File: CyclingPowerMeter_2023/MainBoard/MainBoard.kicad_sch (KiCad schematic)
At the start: 34 parts, among them J1 Conn_01x01, J10 S2B-PH-SM4-TB_LF__SN_, J11 Conn_01x01, J12 Conn_01x01, J2 Conn_01x01, J3 Conn_01x01, J4 Conn_01x01, J5 Conn_01x01, J6 Conn_01x01, J7 Conn_01x01, J8 Conn_01x01, J9 BLA05-05S30, SW1 RS_PRO_PCB_Slide_Switch_SPDT_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, U1 ADS122U04IPW, U2 Seeed_Studio_XIAO_nRF52840_Se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

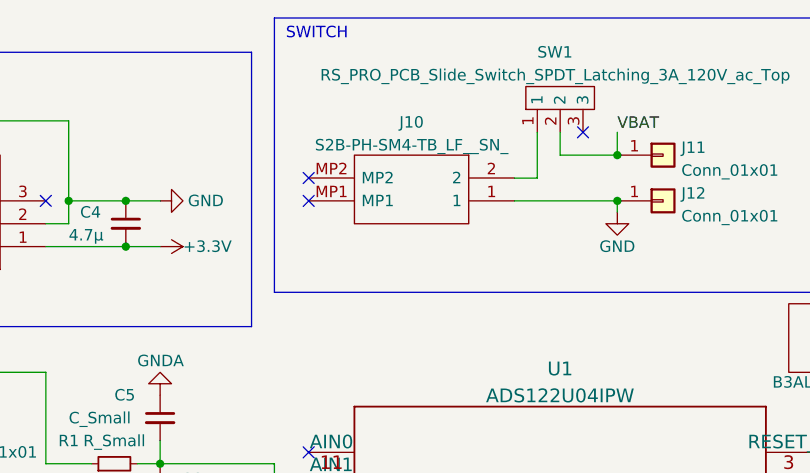
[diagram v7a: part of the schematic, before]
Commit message: 端面スルーホールのオフセットを調整
端面スルーホールのオフセットを調整
PHコネクタの結線を逆にした
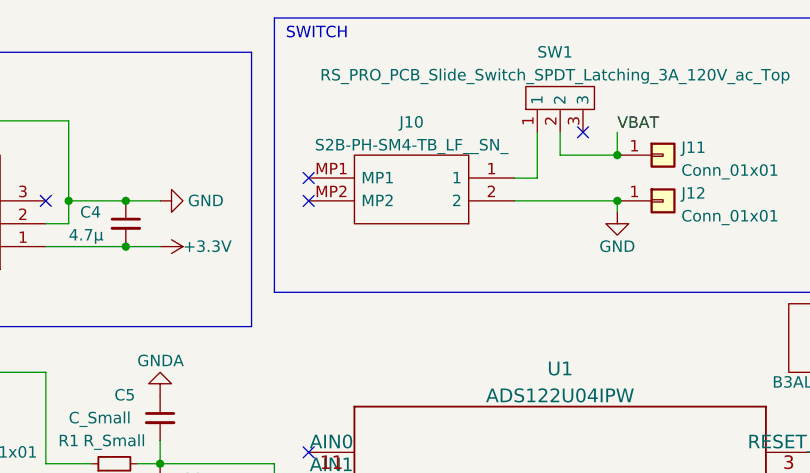
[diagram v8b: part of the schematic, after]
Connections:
- net GND: now also J10.2; no longer J10.1
- net at SW1.1: now also J10.1; no longer J10.2
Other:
- moved on the sheet: J10
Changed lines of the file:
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@@
+    (stroke (width 0) (type default) (color 0 0 0 0))
+  )
+  (wire (pts (xy 142.24 55.88) (xy 153.67 55.88))
     (stroke (width 0) (type default) (color 0 0 0 0))
   )
@@
     (stroke (width 0) (type default) (color 0 0 0 0))
   )
+  (wire (pts (xy 102.87 90.17) (xy 102.87 92.71))
+    (stroke (width 0) (type default) (color 0 0 0 0))
+  )
+  (wire (pts (xy 176.53 116.84) (xy 175.26 116.84))
+    (stroke (width 0) (type default) (color 0 0 0 0))
+  )
+  (wire (pts (xy 144.78 48.26) (xy 144.78 53.34))
+    (stroke (width 0) (type default) (color 0 0 0 0))
+  )
+  (wire (pts (xy 99.06 55.88) (xy 102.87 55.88))
+    (stroke (width 0) (type default) (color 0 0 0 0))
+  )
+  (wire (pts (xy 115.57 90.17) (xy 115.57 88.9))
+    (stroke (width 0) (type default) (color 0 0 0 0))
+  )
+  (wire (pts (xy 92.71 58.42) (xy 92.71 55.88))
+    (stroke (width 0) (type default) (color 0 0 0 0))
+  )
+  (wire (pts (xy 191.77 63.5) (xy 193.04 63.5))
+    (stroke (width 0) (type default) (color 0 0 0 0))
+  )
+  (polyline (pts (xy 115.57 35.56) (xy 176.53 35.56))
+    (stroke (width 0) (type default) (color 0 0 0 0))
+  )
+  (wire (pts (xy 73.66 46.99) (xy 92.71 46.99))
+    (stroke (width 0) (type default) (color 0 0 0 0))
+  )
+  (wire (pts (xy 41.91 55.88) (xy 48.26 55.88))
+    (stroke (width 0) (type default) (color 0 0 0 0))
+  )
+  (wire (pts (xy 64.77 87.63) (xy 72.39 87.63))
+    (stroke (width 0) (type default) (color 0 0 0 0))
+  )
+  (wire (pts (xy 184.15 104.14) (xy 186.69 104.14))
+    (stroke (width 0) (type default) (color 0 0 0 0))
+  )
+  (wire (pts (xy 72.39 87.63) (xy 74.93 87.63))
+    (stroke (width 0) (type default) (color 0 0 0 0))
+  )
+  (wire (pts (xy 187.96 72.39) (xy 190.5 72.39))
+    (stroke (width 0) (type default) (color 0 0 0 0))
+  )
+  (wire (pts (xy 147.32 48.26) (xy 147.32 50.8))
+    (stroke (width 0) (type default) (color 0 0 0 0))
+  )
+  (wire (pts (xy 52.07 87.63) (xy 55.88 83.82))
+    (stroke (width 0) (type default) (color 0 0 0 0))
+  )
+  (polyline (pts (xy 33.02 39.37) (xy 33.02 69.85))
+    (stroke (width 0) (type default) (color 0 0 0 0))
+  )
   (wire (pts (xy 142.24 53.34) (xy 144.78 53.34))
-    (stroke (width 0) (type default) (color 0 0 0 0))
-  )
-  (wire (pts (xy 102.87 90.17) (xy 102.87 92.71))
-    (stroke (width 0) (type default) (color 0 0 0 0))
-  )
-  (wire (pts (xy 176.53 116.84) (xy 175.26 116.84))
-    (stroke (width 0) (type default) (color 0 0 0 0))
-  )
-  (wire (pts (xy 144.78 48.26) (xy 144.78 53.34))
-    (stroke (width 0) (type default) (color 0 0 0 0))
-  )
-  (wire (pts (xy 142.24 55.88) (xy 153.67 55.88))
-    (stroke (width 0) (type default) (color 0 0 0 0))
-  )
-  (wire (pts (xy 99.06 55.88) (xy 102.87 55.88))
-    (stroke (width 0) (type default) (color 0 0 0 0))
-  )
-  (wire (pts (xy 115.57 90.17) (xy 115.57 88.9))
-    (stroke (width 0) (type default) (color 0 0 0 0))
-  )
-  (wire (pts (xy 92.71 58.42) (xy 92.71 55.88))
-    (stroke (width 0) (type default) (color 0 0 0 0))
-  )
-  (wire (pts (xy 191.77 63.5) (xy 193.04 63.5))
-    (stroke (width 0) (type default) (color 0 0 0 0))
-  )
-  (polyline (pts (xy 115.57 35.56) (xy 176.53 35.56))
-    (stroke (width 0) (type default) (color 0 0 0 0))
-  )
-  (wire (pts (xy 73.66 46.99) (xy 92.71 46.99))
-    (stroke (width 0) (type default) (color 0 0 0 0))
-  )
-  (wire (pts (xy 41.91 55.88) (xy 48.26 55.88))
-    (stroke (width 0) (type default) (color 0 0 0 0))
-  )
-  (wire (pts (xy 64.77 87.63) (xy 72.39 87.63))
-    (stroke (width 0) (type default) (color 0 0 0 0))
-  )
-  (wire (pts (xy 184.15 104.14) (xy 186.69 104.14))
-    (stroke (width 0) (type default) (color 0 0 0 0))
-  )
-  (wire (pts (xy 72.39 87.63) (xy 74.93 87.63))
-    (stroke (width 0) (type default) (color 0 0 0 0))
-  )
-  (wire (pts (xy 187.96 72.39) (xy 190.5 72.39))
-    (stroke (width 0) (type default) (color 0 0 0 0))
-  )
-  (wire (pts (xy 147.32 48.26) (xy 147.32 50.8))
-    (stroke (width 0) (type default) (color 0 0 0 0))
-  )
-  (wire (pts (xy 52.07 87.63) (xy 55.88 83.82))
-    (stroke (width 0) (type default) (color 0 0 0 0))
-  )
-  (polyline (pts (xy 33.02 39.37) (xy 33.02 69.85))
     (stroke (width 0) (type default) (color 0 0 0 0))
   )
@@
     (pin "2")
   )
-  (symbol (lib_id "S2B-PH-SM4-TB:S2B-PH-SM4-TB_LF__SN_") (at 142.24 53.34 0) (mirror y) (unit 1)
+  (symbol (lib_id "S2B-PH-SM4-TB:S2B-PH-SM4-TB_LF__SN_") (at 142.24 55.88 180) (unit 1)
     (in_bom yes) (on_board yes) (fields_autoplaced)
     (property "Reference" "J10" (id 0) (at 130.81 47.151 0))
     (property "Value" "S2B-PH-SM4-TB_LF__SN_" (id 1) (at 130.81 49.6879 0))
-    (property "Footprint" "S2B-PH-SM4-TB:S2B-PH-SM4-TB" (id 2) (at 123.19 50.8 0)
-      (effects (font (size 1.27 1.27)) (justify left) hide)
-    )
-    (property "Datasheet" "https://www.jst-mfg.com/product/pdf/eng/ePH.pdf" (id 3) (at 123.19 53.34 0)
-      (effects (font (size 1.27 1.27)) (justify left) hide)
-    )
-    (property "Description" "Conn Shrouded Header (4 Sides) HDR 2 POS 2mm Solder RA Side Entry SMD T/R" (id 4) (at 123.19 55.88 0)
-      (effects (font (size 1.27 1.27)) (justify left) hide)
-    )
-    (property "Height" "6.6" (id 5) (at 123.19 58.42 0)
-      (effects (font (size 1.27 1.27)) (justify left) hide)
-    )
-    (property "Manufacturer_Name" "JST (JAPAN SOLDERLESS TERMINALS)" (id 6) (at 123.19 60.96 0)
-      (effects (font (size 1.27 1.27)) (justify left) hide)
-    )
-    (property "Manufacturer_Part_Number" "S2B-PH-SM4-TB(LF)(SN)" (id 7) (at 123.19 63.5 0)
-      (effects (font (size 1.27 1.27)) (justify left) hide)
-    )
-    (property "Mouser Part Number" "" (id 8) (at 123.19 66.04 0)
-      (effects (font (size 1.27 1.27)) (justify left) hide)
-    )
-    (property "Mouser Price/Stock" "" (id 9) (at 123.19 68.58 0)
-      (effects (font (size 1.27 1.27)) (justify left) hide)
-    )
-    (property "Arrow Part Number" "S2B-PH-SM4-TB(LF)(SN)" (id 10) (at 123.19 71.12 0)
-      (effects (font (size 1.27 1.27)) (justify left) hide)
-    )
-    (property "Arrow Price/Stock" "https://www.arrow.com/en/products/s2b-ph-sm4-tb-lf-sn/jst-manufacturing" (id 11) (at 123.19 73.66 0)
-      (effects (font (size 1.27 1.27)) (justify left) hide)
-    )
-    (property "Mouser Testing Part Number" "" (id 12) (at 123.19 76.2 0)
-      (effects (font (size 1.27 1.27)) (justify left) hide)
-    )
-    (property "Mouser Testing Price/Stock" "" (id 13) (at 123.19 78.74 0)
-      (effects (font (size 1.27 1.27)) (justify left) hide)
-    )
+    (property "Footprint" "S2B-PH-SM4-TB:S2B-PH-SM4-TB" (id 2) (at 123.19 58.42 0)
+      (effects (font (size 1.27 1.27)) (justify left) hide)
+    )
+    (property "Datasheet" "https://www.jst-mfg.com/product/pdf/eng/ePH.pdf" (id 3) (at 123.19 55.88 0)
+      (effects (font (size 1.27 1.27)) (justify left) hide)
+    )
+    (property "Description" "Conn Shrouded Header (4 Sides) HDR 2 POS 2mm Solder RA Side Entry SMD T/R" (id 4) (at 123.19 53.34 0)
+      (effects (font (size 1.27 1.27)) (justify left) hide)
+    )
+    (property "Height" "6.6" (id 5) (at 123.19 50.8 0)
+      (effects (font (size 1.27 1.27)) (justify left) hide)
+    )
+    (property "Manufacturer_Name" "JST (JAPAN SOLDERLESS TERMINALS)" (id 6) (at 123.19 48.26 0)
+      (effects (font (size 1.27 1.27)) (justify left) hide)
+    )
+    (property "Manufacturer_Part_Number" "S2B-PH-SM4-TB(LF)(SN)" (id 7) (at 123.19 45.72 0)
+      (effects (font (size 1.27 1.27)) (justify left) hide)
+    )
+    (property "Mouser Part Number" "" (id 8) (at 123.19 43.18 0)
+      (effects (font (size 1.27 1.27)) (justify left) hide)
+    )
+    (property "Mouser Price/Stock" "" (id 9) (at 123.19 40.64 0)
+      (effects (font (size 1.27 1.27)) (justify left) hide)
+    )
+    (property "Arrow Part Number" "S2B-PH-SM4-TB(LF)(SN)" (id 10) (at 123.19 38.1 0)
+      (effects (font (size 1.27 1.27)) (justify left) hide)
+    )
+    (property "Arrow Price/Stock" "https://www.arrow.com/en/products/s2b-ph-sm4-tb-lf-sn/jst-manufacturing" (id 11) (at 123.19 35.56 0)
+      (effects (font (size 1.27 1.27)) (justify left) hide)
+    )
+    (property "Mouser Testing Part Number" "" (id 12) (at 123.19 33.02 0)
+      (effects (font (size 1.27 1.27)) (justify left) hide)
+    )
+    (property "Mouser Testing Price/Stock" "" (id 13) (at 123.19 30.48 0)
+      (effects (font (size 1.27 1.27)) (justify left) hide)
+    )
